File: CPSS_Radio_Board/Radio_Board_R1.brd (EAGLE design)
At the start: 68.1 x 55 mm, 46 parts, among them IC1 FT2232D, T1 BCW81SMD, X1 BU-SMA-V, X2 MINI-USB-UX60-MB-5S8

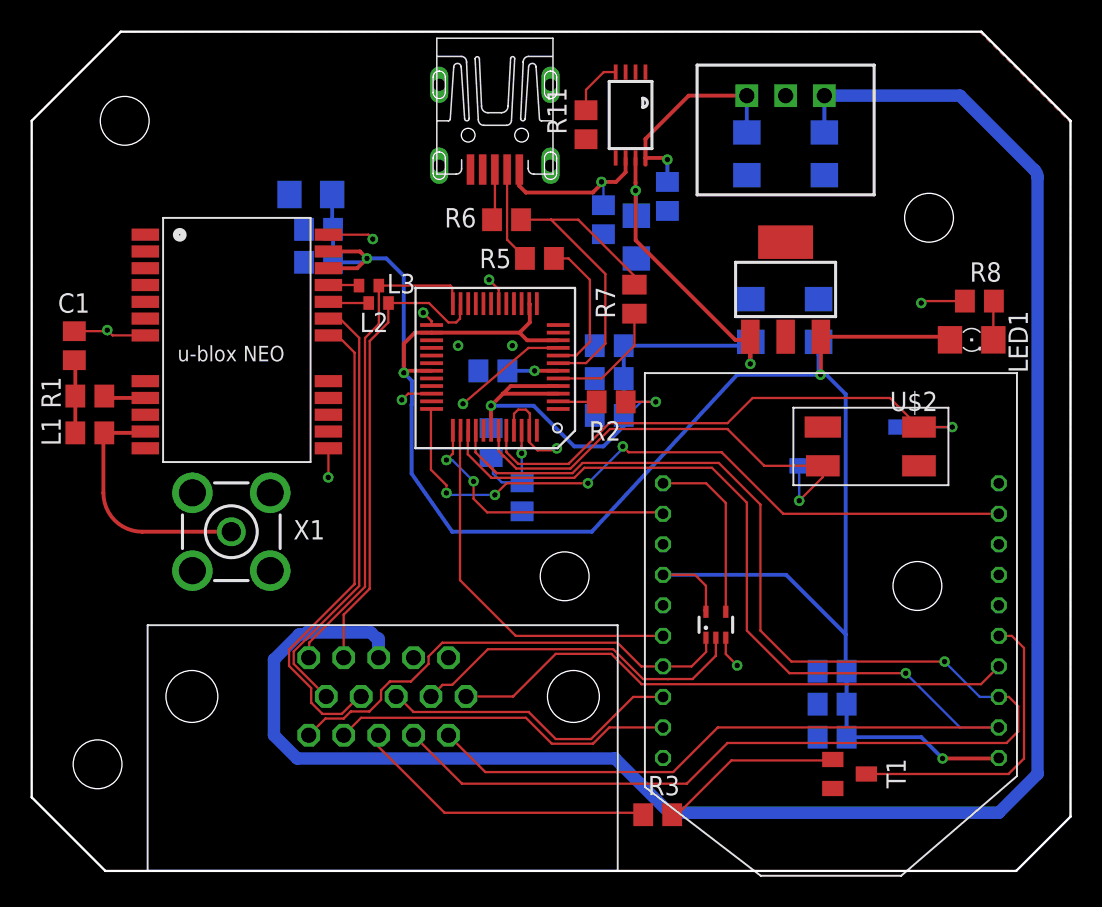
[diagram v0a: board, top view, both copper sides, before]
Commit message: Added BOM and PCB GND connections for crystal
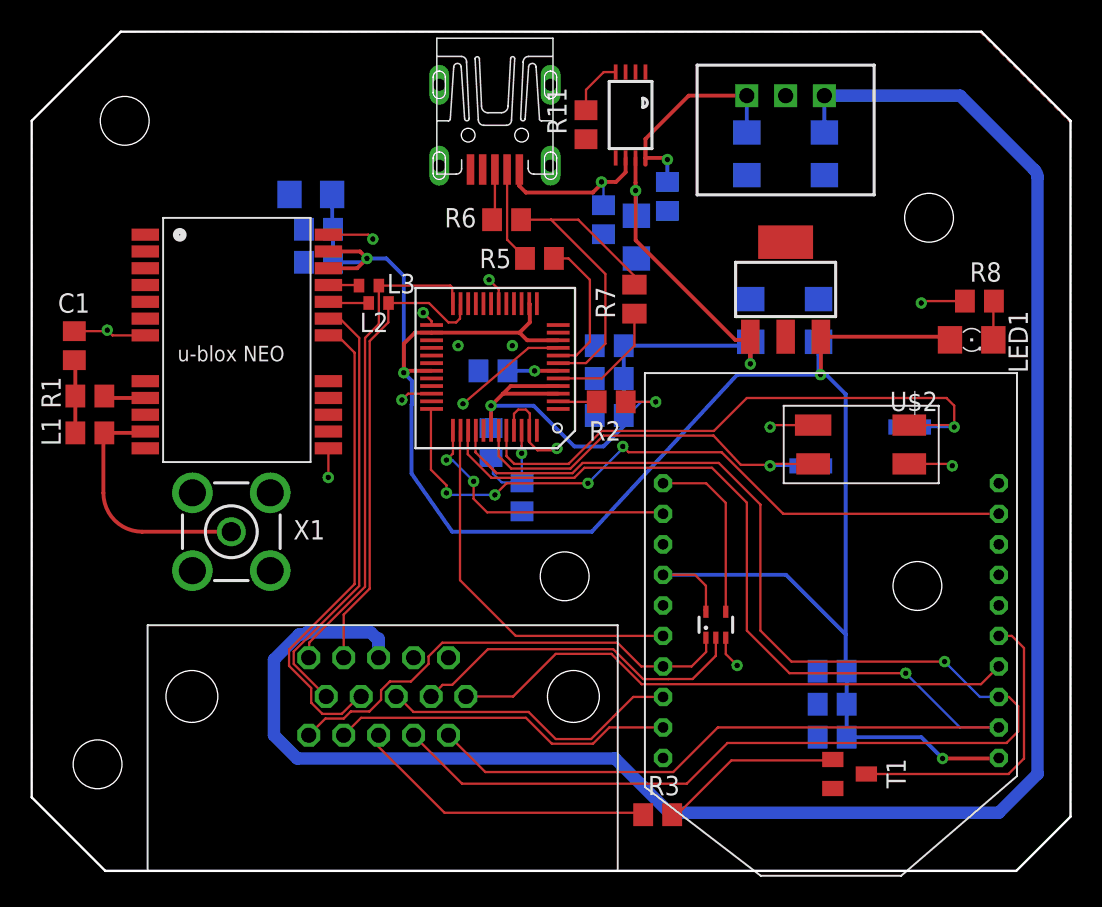
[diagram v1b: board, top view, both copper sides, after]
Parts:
- moved U$8 0.65 mm to (54.7, 28.2)
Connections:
- net GND: now also U$8.2, U$8.4
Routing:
- net GND: track 33.8 -> 39.6 mm, vias 12 -> 14
- net N$4: track 35.5 -> 39.7 mm
- net N$3: track 30.5 -> 26.3 mm
